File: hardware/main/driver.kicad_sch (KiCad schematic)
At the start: 11 parts, among them U501 PDSE1-S5-S24-S, U502 1EDI60N12AFXUMA1

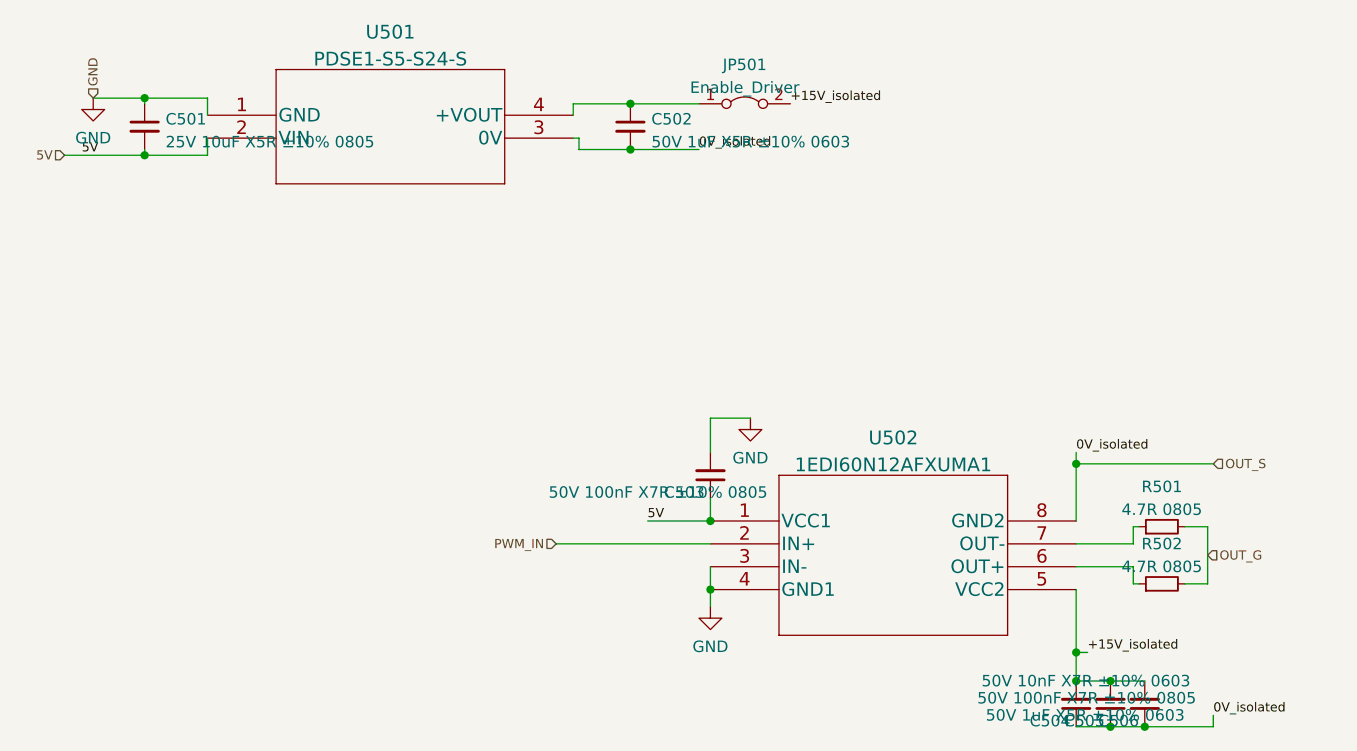
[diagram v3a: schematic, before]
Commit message: Schematics: Run DRC and fix errors and some warnings, also added Zenite kicad library repo as submodule
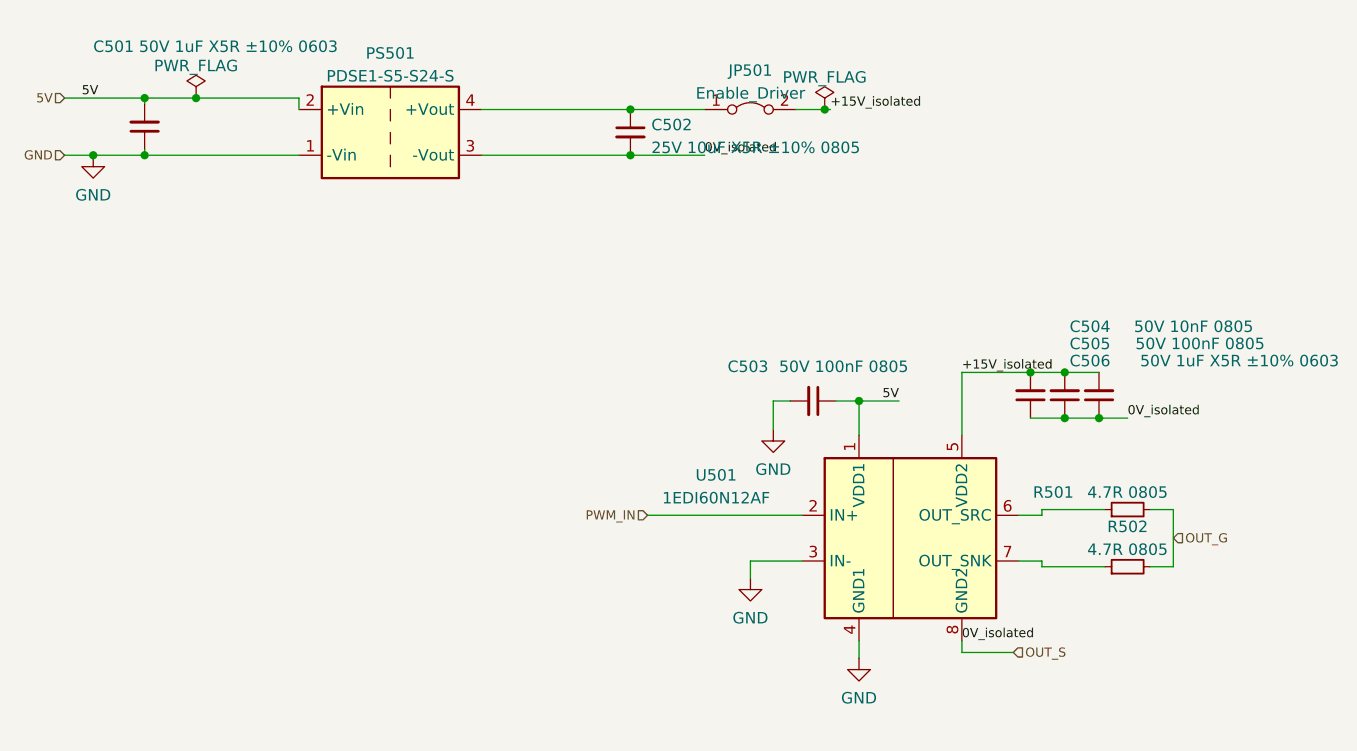
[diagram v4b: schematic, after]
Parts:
- removed U501: PDSE1-S5-S24-S, symbol zenite:PDSE1-S5-S24-S
- removed U502: 1EDI60N12AFXUMA1, symbol zenite:1EDI60N12AFXUMA1
- added PS501: PDSE1-S5-S24-S, Converter_DCDC:Converter_DCDC_Murata_MEE3SxxxxSC_THT, symbol Converter_DCDC:MEE3S0512SC
- added U501: 1EDI60N12AF, Package_SO:SOIC-8_3.9x4.9mm_P1.27mm, symbol zenite:1EDI60N12AF
- C501: renamed from C502; footprint (none) -> Capacitor_SMD:C_0603_1608Metric_Pad1.08x0.95mm_HandSolder
- C502: renamed from C501; footprint (none) -> Capacitor_SMD:C_0805_2012Metric_Pad1.18x1.45mm_HandSolder
- C503, C505: value 50V 100nF X7R ±10% 0805 -> 50V 100nF 0805; footprint (none) -> Capacitor_SMD:C_0805_2012Metric_Pad1.18x1.45mm_HandSolder
- C504: value 50V 10nF X7R ±10% 0603 -> 50V 10nF 0805; footprint (none) -> Capacitor_SMD:C_0805_2012Metric_Pad1.18x1.45mm_HandSolder
- C506: footprint (none) -> Capacitor_SMD:C_0603_1608Metric_Pad1.08x0.95mm_HandSolder
- JP501: footprint (none) -> Jumper:SolderJumper-2_P1.3mm_Open_TrianglePad1.0x1.5mm
- R501, R502: footprint (none) -> Resistor_SMD:R_0805_2012Metric_Pad1.20x1.40mm_HandSolder
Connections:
- net +15V_isolated: now also U501.5 (VDD2)
- net 5V: now also C501.2, PS501.2 (+Vin), U501.1 (VDD1); no longer C502.2
- net GND: now also C501.1, PS501.1 (-Vin), U501.3 (IN-), U501.4 (GND1); no longer C502.1
- net OUT_S: now also C502.2, PS501.3 (-Vout), U501.8 (GND2); no longer C501.2
- net PWM_IN: now also U501.2 (IN+)
- net at JP501.1 (A): now also C502.1, PS501.4 (+Vout); no longer C501.1
- net at R502.1: now also U501.7 (OUT_SNK)
- net at R501.1: now also U501.6 (OUT_SRC)
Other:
- moved on the sheet: C501, C502, C503, C504, C505, C506, JP501, R501, R502

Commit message: Layout: Fist version of power stage
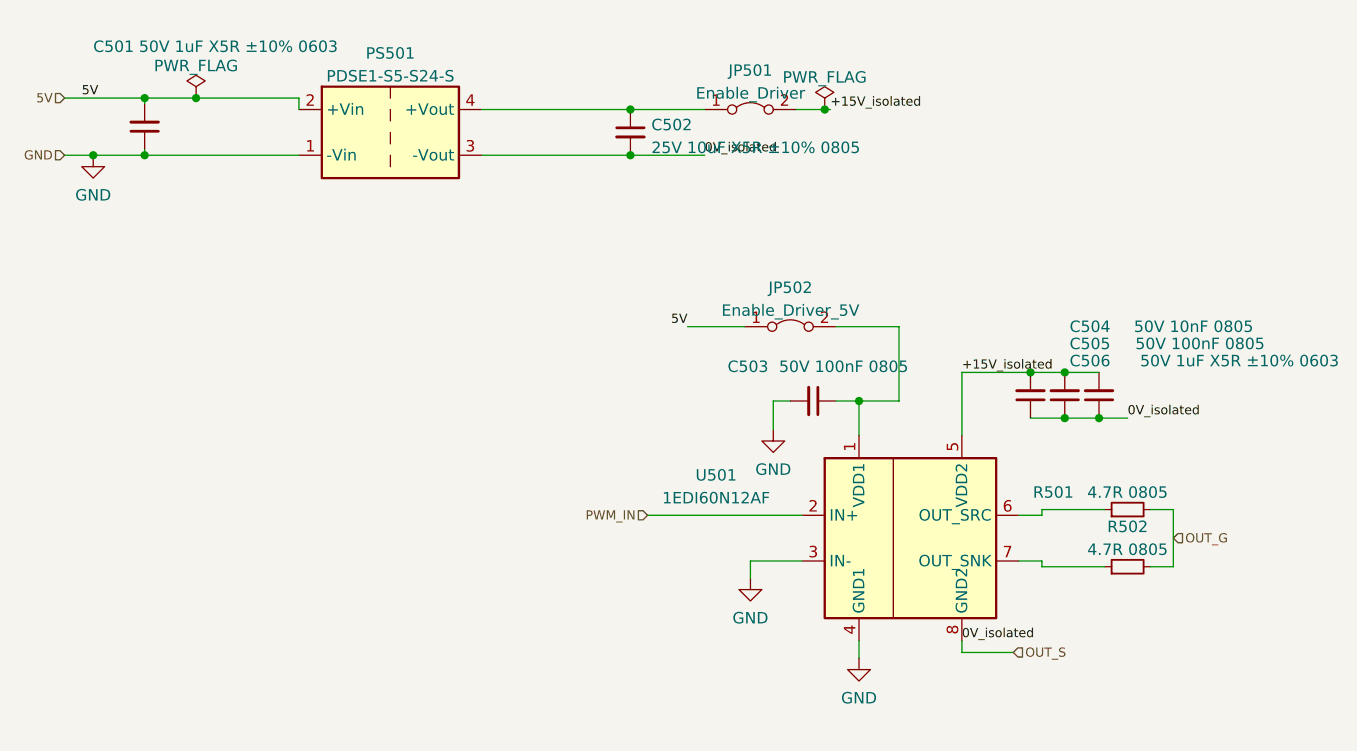
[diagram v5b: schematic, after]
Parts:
- added JP502: Enable_Driver_5V, Zenite:SolderJumper-2_P0.5mm_Open_TrianglePad0.5x0.5mm, symbol Jumper:Jumper_2_Bridged
- JP501: footprint Jumper:SolderJumper-2_P1.3mm_Open_TrianglePad1.0x1.5mm -> Zenite:SolderJumper-2_P0.5mm_Open_TrianglePad0.5x0.5mm
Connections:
- net 5V: now also JP502.1 (A); no longer C503.1, U501.1 (VDD1)
- new net: C503.1, JP502.2 (B), U501.1 (VDD1)
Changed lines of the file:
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@@
+    (stroke (width 0) (type default) (color 0 0 0 0))
+  )
+  (wire (pts (xy 133.35 89.535) (xy 133.35 97.79))
     (stroke (width 0) (type default) (color 0 0 0 0))
   )
@@
     (stroke (width 0) (type default) (color 0 0 0 0))
   )
+  (wire (pts (xy 109.855 89.535) (xy 116.205 89.535))
+    (stroke (width 0) (type default) (color 0 0 0 0))
+  )
   (wire (pts (xy 55.245 64.135) (xy 66.675 64.135))
     (stroke (width 0) (type default) (color 0 0 0 0))
@@
     (stroke (width 0) (type default) (color 0 0 0 0))
   )
+  (wire (pts (xy 126.365 89.535) (xy 133.35 89.535))
+    (stroke (width 0) (type default) (color 0 0 0 0))
+  )
   (wire (pts (xy 103.505 70.485) (xy 111.76 70.485))
     (stroke (width 0) (type default) (color 0 0 0 0))
@@
     (stroke (width 0) (type default) (color 0 0 0 0))
   )
-  (label "5V" (at 133.35 97.79 180)
+  (label "5V" (at 109.855 89.535 180)
     (effects (font (size 1.016 1.016)) (justify right bottom))
   )
@@
     (pin "2")
   )
+  (symbol (lib_id "Jumper:Jumper_2_Bridged") (at 121.285 89.535 0) (unit 1)
+    (in_bom yes) (on_board yes) (fields_autoplaced)
+    (property "Reference" "JP502" (id 0) (at 121.285 85.2002 0))
+    (property "Value" "Enable_Driver_5V" (id 1) (at 121.285 87.7371 0))
+    (property "Footprint" "Zenite:SolderJumper-2_P0.5mm_Open_TrianglePad0.5x0.5mm" (id 2) (at 121.285 89.535 0)
+      (effects (font (size 1.27 1.27)) hide)
+    )
+    (property "Datasheet" "~" (id 3) (at 121.285 89.535 0)
+      (effects (font (size 1.27 1.27)) hide)
+    )
+    (pin "1")
+    (pin "2")
+  )
   (symbol (lib_id "power:GND") (at 128.905 126.365 0) (unit 1)
     (in_bom yes) (on_board yes) (fields_autoplaced)
@@
     (property "Reference" "JP501" (id 0) (at 116.84 61.0702 0))
     (property "Value" "Enable_Driver" (id 1) (at 116.84 63.6071 0))
-    (property "Footprint" "Jumper:SolderJumper-2_P1.3mm_Open_TrianglePad1.0x1.5mm" (id 2) (at 116.84 65.405 0)
-      (effects (font (size 1.27 1.27)) hide)
-    )
+    (property "Footprint" "Zenite:SolderJumper-2_P0.5mm_Open_TrianglePad0.5x0.5mm" (id 2) (at 116.84 65.405 0)
+      (effects (font (size 1.27 1.27)) hide)
+    )

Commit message: Layout: Organize and initialize routing of control
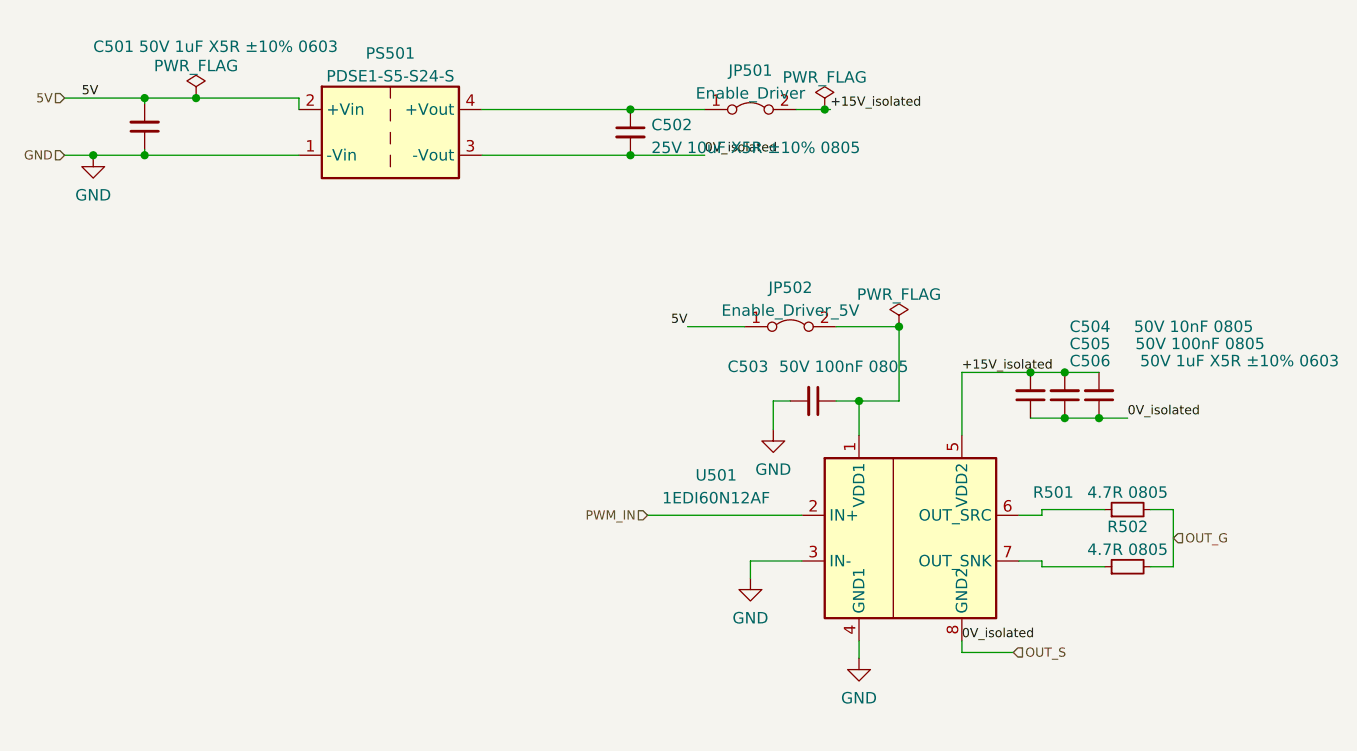
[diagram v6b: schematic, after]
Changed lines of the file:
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@@
   (junction (at 103.505 70.485) (diameter 0) (color 0 0 0 0)
+  )
+  (junction (at 133.35 89.535) (diameter 0) (color 0 0 0 0)
   )
   (junction (at 43.815 70.485) (diameter 0) (color 0 0 0 0)
@@
     (effects (font (size 1.016 1.016)) (justify left))
   )
+  (symbol (lib_id "power:PWR_FLAG") (at 133.35 89.535 0) (unit 1)
+    (in_bom yes) (on_board yes) (fields_autoplaced)
+    (property "Reference" "#FLG0101" (id 0) (at 133.35 87.63 0)
+      (effects (font (size 1.27 1.27)) hide)
+    )
+    (property "Value" "PWR_FLAG" (id 1) (at 133.35 85.9592 0))
+    (property "Footprint" "" (id 2) (at 133.35 89.535 0)
+      (effects (font (size 1.27 1.27)) hide)
+    )
+    (property "Datasheet" "~" (id 3) (at 133.35 89.535 0)
+      (effects (font (size 1.27 1.27)) hide)
+    )
+    (pin "1")
+  )
   (symbol (lib_id "Device:C_Small") (at 49.53 67.31 0) (mirror x) (unit 1)

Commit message: Layout: Connect all unconected nets, and fix all DRC errors
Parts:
- JP501, JP502: footprint Zenite:SolderJumper-2_P0.5mm_Open_TrianglePad0.5x0.5mm -> Zenite:SolderJumper-2_P0.5mm_Open_TrianglePad0.8x0.5mm
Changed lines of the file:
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@@
     (property "Reference" "JP502" (id 0) (at 121.285 85.2002 0))
     (property "Value" "Enable_Driver_5V" (id 1) (at 121.285 87.7371 0))
-    (property "Footprint" "Zenite:SolderJumper-2_P0.5mm_Open_TrianglePad0.5x0.5mm" (id 2) (at 121.285 89.535 0)
+    (property "Footprint" "Zenite:SolderJumper-2_P0.5mm_Open_TrianglePad0.8x0.5mm" (id 2) (at 121.285 89.535 0)
       (effects (font (size 1.27 1.27)) hide)
     )
@@
     (property "Reference" "JP501" (id 0) (at 116.84 61.0702 0))
     (property "Value" "Enable_Driver" (id 1) (at 116.84 63.6071 0))
-    (property "Footprint" "Zenite:SolderJumper-2_P0.5mm_Open_TrianglePad0.5x0.5mm" (id 2) (at 116.84 65.405 0)
+    (property "Footprint" "Zenite:SolderJumper-2_P0.5mm_Open_TrianglePad0.8x0.5mm" (id 2) (at 116.84 65.405 0)
       (effects (font (size 1.27 1.27)) hide)
     )
